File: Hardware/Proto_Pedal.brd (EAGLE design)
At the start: 85.1 x 110.5 mm, 98 parts, among them J1 5.5x2.1mm Barrel, Q1 MMBT2222A, Q2 MOSFET-NCHANNEL2N7002PW, Q3 30V, 2.5A

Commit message: PCB Ready for protos
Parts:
- removed JP68: FX IN, SparkFun-Connectors:1X01NS
- added C2: 100uF, SparkFun-Capacitors:PANASONIC_D
- added D2: RED, SparkFun-LED:LED-0603
- added JP86: FX OUT, SparkFun-Connectors:1X03_NO_SILK
- added JP87: FX IN, SparkFun-Connectors:1X03_NO_SILK
- added LOGO1: SFE_LOGO_NAME_FLAME.2_INCH, SparkFun-Aesthetics:SFE_LOGO_NAME_FLAME_.2
- added LOGO3: OSHW-LOGOL, SparkFun-Aesthetics:OSHW-LOGO-L
- added R4, R5: 100k, SparkFun-Resistors:0603-RES
- added SJ1: disable LED, SparkFun-Passives:PAD-JUMPER-2-NC_BY_PASTE_YES_SILK_FULL_BOX
- added STANDOFF1, STANDOFF2, STANDOFF3, STANDOFF4: STAND-OFF, SparkFun-Electromechanical:STAND-OFF
- JP1: value AUDIO-JACK4-.25-HORIZ-TRS -> INPUT JACK
- JP2: value AUDIO-JACK4-.25-HORIZ-TRS -> OUTPUT JACK
- JP69: value FX OUT -> (none); device SparkFun-Connectors:1X01NS -> SparkFun-Connectors:1X03_NO_SILK
- S1: value (none) -> DPDT Stomp
- U1: value (none) -> TLE2426
- moved JP69 68.1 mm to (40.6, 94.0), turned to 270 degrees
- moved Q1 8.89 mm to (57.1, 7.62)
- moved R1 7.62 mm to (57.1, 14.0)
- moved C1 7.18 mm to (26.7, 104.1)
- moved D1 6.35 mm to (57.1, 3.81)
- moved Q3 5.68 mm to (40.6, 104.1)
- moved JP67 5.08 mm to (67.3, 22.9), turned to 90 degrees
- moved R3 3.59 mm to (36.8, 101.6)
- moved U1 2.84 mm to (31.8, 104.1), turned to 0 degrees
- moved JP66 2.54 mm to (3.81, 72.4)
- moved JP72 2.54 mm to (3.81, 83.8)
- moved JP73 2.54 mm to (16.5, 83.8)
- moved JP75 2.54 mm to (29.2, 83.8)
- moved JP78 2.54 mm to (2.54, 50.8)
- moved JP79 2.54 mm to (41.9, 83.8)
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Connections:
- new net N$25: D2.A, SJ1.2
- net FX_IN: now also JP87.1, JP87.2, JP87.3, R5.2; no longer JP68.1
- net FX_OUT: now also JP86.1, JP86.2, JP86.3, R4.2; no longer JP69.1
- net GND: now also C2.-, JP69.1, R4.1, R5.1
- net LEDA: now also SJ1.1
- net LEDK: now also D2.C
- net VCC: now also C2.+, JP69.3
- net VREF: now also JP69.2
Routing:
- net VCC: track 0.00 -> 350.0 mm, vias 0 -> 3
- net GND: track 0.00 -> 190.0 mm, vias 0 -> 52
- net N$71: track 0.00 -> 184.5 mm, vias 0 -> 1
- net VBATT: track 0.00 -> 174.3 mm
- net N$69: track 0.00 -> 165.8 mm, vias 0 -> 1
- net N$70: track 0.00 -> 121.7 mm, vias 0 -> 1
- net VREF: track 0.00 -> 96.6 mm, vias 0 -> 1
- net FX_IN: track 0.00 -> 77.1 mm
- net N$90: track 0.00 -> 73.7 mm
- net N$89: track 0.00 -> 73.7 mm
- net FX_OUT: track 0.00 -> 58.7 mm
- net N$76: track 0.00 -> 28.7 mm, vias 0 -> 1
- net LEDK: track 0.00 -> 26.6 mm, vias 0 -> 1
- net LEDA: track 0.00 -> 24.4 mm, vias 0 -> 1
- net N$65: track 0.00 -> 21.2 mm
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- added copper zone on layer 1, net GND
- added copper zone on layer 16, net GND
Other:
- outline, holes or cut-outs redrawn
- board text added: "Clear SJ1 to disable SMT LED"
- board text added: "Proto Pedal"
- board text added: "SJ1"
- board text removed: "LEDA"
- board text removed: "LEDK"

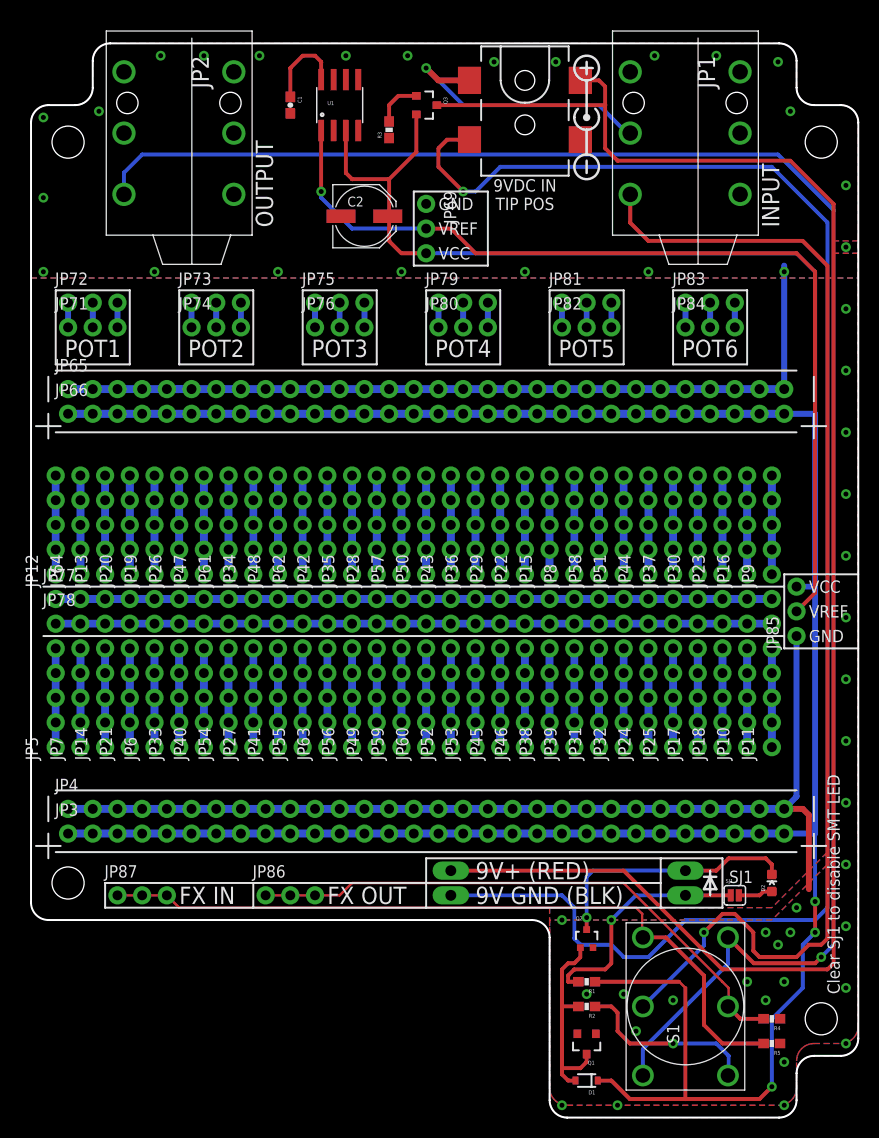
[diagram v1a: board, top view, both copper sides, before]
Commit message: WIP.
Redid bypass switch to 3PDT component with multiple gates.
Removed questionable LED circuit, replaced with an actual switch
section.
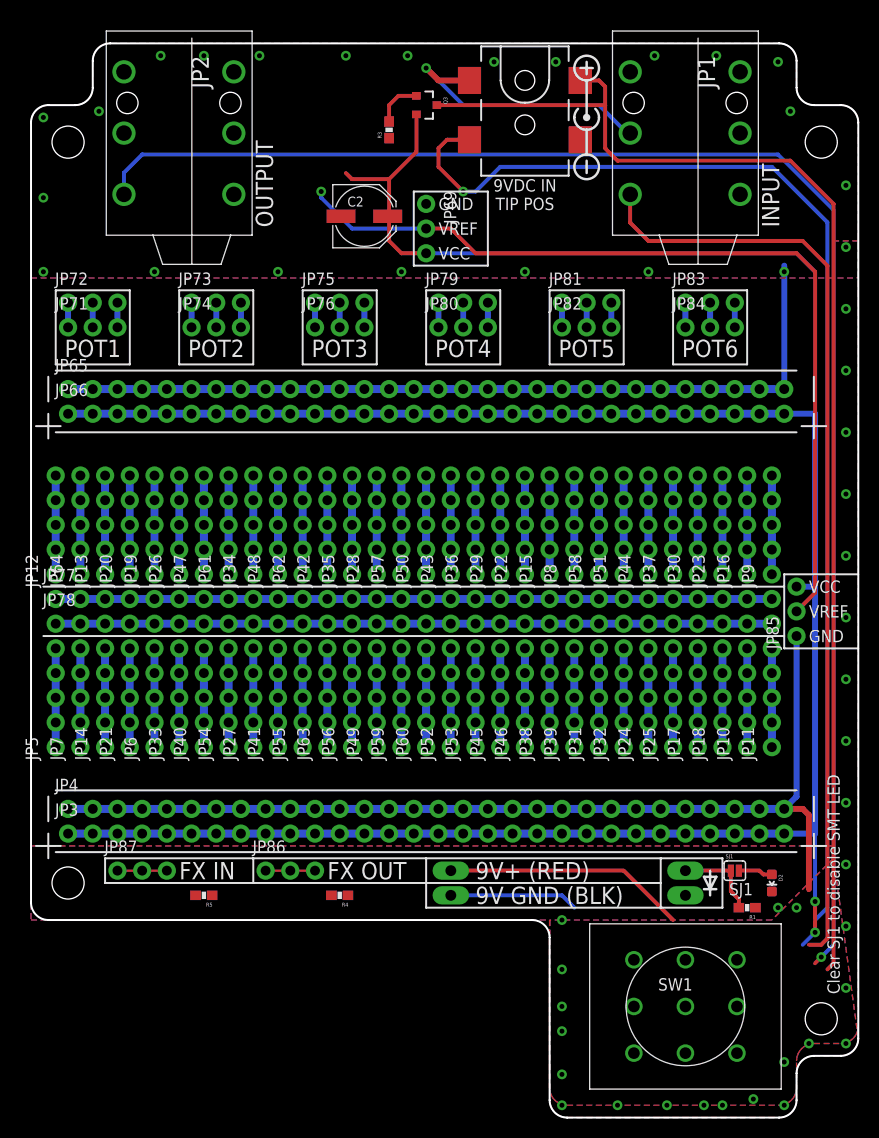
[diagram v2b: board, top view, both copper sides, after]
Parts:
- removed C1: 1.0uF, SparkFun-Capacitors:0603-CAP
- removed D1: BAS16, SparkFun-DiscreteSemi:SOD-323
- removed Q1: MMBT2222A, SparkFun-DiscreteSemi:SOT23-3
- removed Q2: MOSFET-NCHANNEL2N7002PW, SparkFun-DiscreteSemi:SOT323
- removed R2: 10K, SparkFun-Resistors:0603-RES
- removed S1: DPDT Stomp, SparkFun-Electromechanical:STOMP-SWITCH-DPDT
- removed U1: TLE2426, SparkFun-PowerIC:SO08
- added SW1: SWITCH-3PDT, SparkFun-Electromechanical:STOMP-SWITCH-3PDT
- JP3, JP4, JP65, JP66, JP77, JP78: value M30NO_SILK -> (none)
- Q3: value 30V, 2.5A -> 2.5A/30V
- moved R5 60.4 mm to (17.8, 22.9)
- moved R4 46.2 mm to (31.8, 22.9)
- moved R1 18.2 mm to (73.7, 21.6)
- moved JP67 2.54 mm to (67.3, 25.4), turned to 270 degrees
- moved JP86 2.54 mm to (24.1, 25.4)
- moved JP87 2.54 mm to (8.89, 25.4)
- moved SJ1 2.54 mm to (72.4, 25.4)
- turned D2 to 180 degrees
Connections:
- removed net LEDK: D2.C, JP67.2, Q2.3
- removed net N$65: D1.A, Q1.3, Q2.1, R2.2
- removed net N$74: R2.1, S1.P$4
- removed net N$92: C1.1, U1.8
- new net N$35: R1.1, SW1.P$9
- net FX_IN: now also SW1.P$2; no longer S1.P$3
- net FX_OUT: no longer S1.P$5
- net GND: now also D2.C, JP67.2, SW1.P$1; no longer C1.2, Q1.1, Q2.2, U1.2
- net N$70: now also SW1.P$3; no longer S1.P$2
- net N$71: now also SW1.P$5; no longer S1.P$1, S1.P$6
- net VCC: no longer D1.C, R1.1, U1.3
- net VREF: no longer U1.1
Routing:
- net FX_IN: track 77.1 -> 5.08 mm
- net VCC: track 350.0 -> 289.5 mm, vias 3 -> 2
- net FX_OUT: track 58.7 -> 5.08 mm
- net N$69: track 165.8 -> 135.4 mm
- net N$71: track 184.5 -> 156.6 mm
- net LEDK: track 26.6 -> 0.00 mm, vias 1 -> 0
- net N$70: track 121.7 -> 96.4 mm, vias 1 -> 0
- net N$65: track 21.2 -> 0.00 mm
- net N$74: track 19.0 -> 0.00 mm, vias 1 -> 0
- net VBATT: track 174.3 -> 156.3 mm
- net LEDA: track 24.4 -> 8.82 mm, vias 1 -> 0
- net N$92: track 8.75 -> 0.00 mm
- net VREF: track 96.6 -> 90.3 mm

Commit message: More WIP
Many more changes based on prototype review.
-Tip-negative power input.
-uncommited proto space for power regulation.
-Rail splitter removed
-Strain relief near 9V snap
-Some test points on i/O jacks
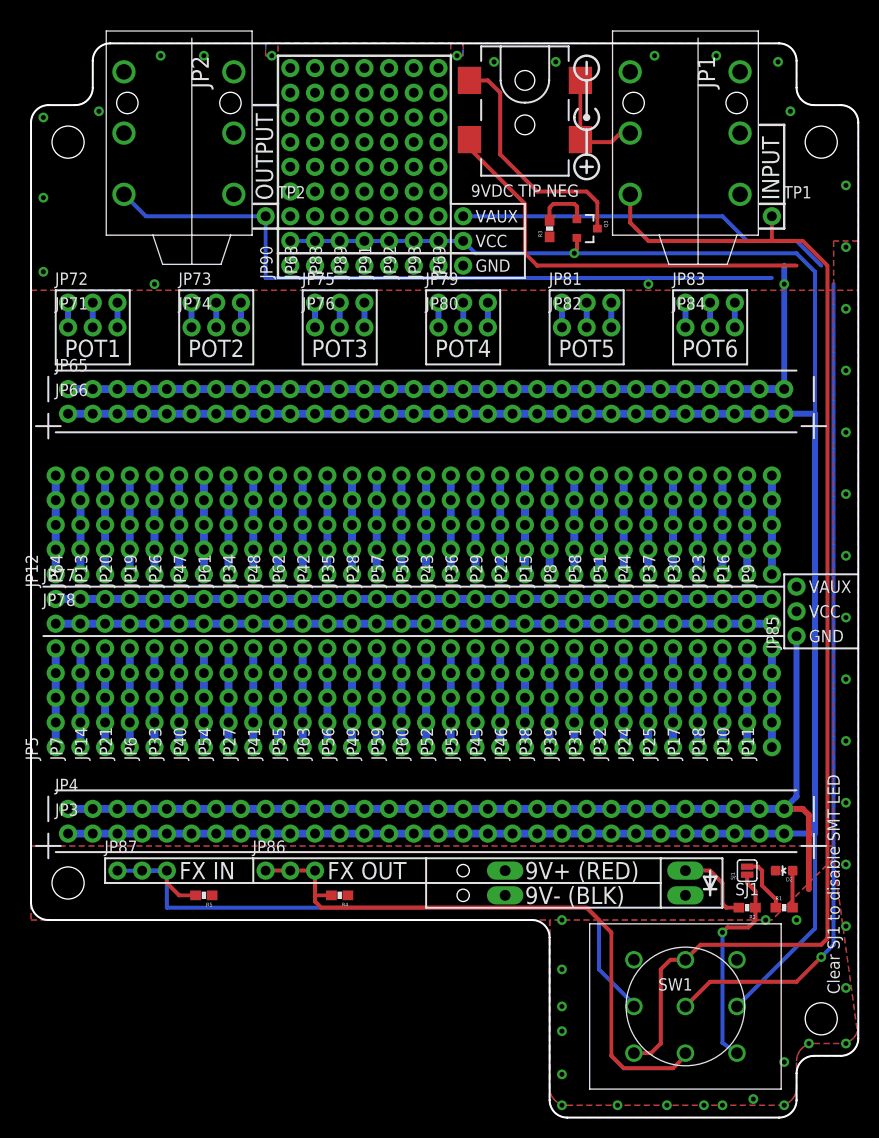
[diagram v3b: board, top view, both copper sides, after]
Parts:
- removed C2: 100uF, SparkFun-Capacitors:PANASONIC_D
- added JP68, JP88, JP89, JP90, JP91, JP92, JP93: (no value), SparkFun-Connectors:1X09_NO_SILK
- added R2: 1K, SparkFun-Resistors:0603-RES
- added TP1: Raw In, SparkFun-Connectors:1X01_NO_SILK
- added TP2: Raw Out, SparkFun-Connectors:1X01_NO_SILK
- J1: value 5.5x2.1mm Barrel -> POWER_JACKSMD_FIXED; device SparkFun-Connectors:POWER_JACK_SMD -> Testing:POWER_JACK_SMD
- moved Q3 20.8 mm to (57.1, 91.4)
- moved R3 19.4 mm to (53.3, 91.4)
- moved LOGO1 17.0 mm to (53.3, 114.3)
- moved JP69 7.41 mm to (44.5, 87.6), turned to 90 degrees
- moved JP70 5.59 mm to (48.8, 25.4)
- moved R1 3.81 mm to (77.5, 21.6), turned to 0 degrees
- moved D2 1.80 mm to (77.5, 25.4), turned to 90 degrees
- moved SJ1 1.27 mm to (73.7, 25.4), turned to 90 degrees
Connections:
- removed net N$69: J1.P$4, JP70.2
- removed net N$76: J1.GND, JP1.RING
- removed net VREF: JP69.2, JP85.2
- new net N$45: J1.P$4, JP70.1
- new net N$55: J1.VIN0, J1.VIN1, JP1.RING, JP70.2
- new net N$65: R1.1, SJ1.2
- new net VAUX: JP69.3, JP85.3
- net FX_OUT: now also SW1.P$6
- net GND: now also JP68.1, JP88.1, JP89.1, JP90.1, JP91.1, JP92.1, JP93.1; no longer C2.-
- net LEDA: now also R2.2; no longer R1.2, SJ1.1
- net N$25: now also R1.2; no longer SJ1.2
- net N$35: now also R2.1, SJ1.1; no longer R1.1
- net N$70: now also SW1.P$4, TP1.1
- net N$71: now also TP2.1
- net VBATT: now also J1.GND; no longer J1.VIN0, JP70.1
- net VCC: now also JP68.2, JP69.2, JP85.2, JP88.2, JP89.2, JP90.2, JP91.2, JP92.2, JP93.2, SW1.P$8; no longer C2.+, JP69.3, JP85.3
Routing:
- net N$69: track 135.4 -> 0.00 mm, vias 1 -> 0
- net VBATT: track 156.3 -> 24.8 mm
- net VREF: track 90.3 -> 0.00 mm, vias 1 -> 0
- net FX_IN: track 5.08 -> 71.5 mm
- net FX_OUT: track 5.08 -> 63.4 mm
- net N$45: track 0.00 -> 42.5 mm
- net VAUX: track 0.00 -> 38.9 mm
- net N$70: track 96.4 -> 126.0 mm
- net N$76: track 28.7 -> 0.00 mm, vias 1 -> 0
- net N$35: track 0.00 -> 22.2 mm, vias 0 -> 1
- net N$55: track 0.00 -> 11.7 mm
- net N$65: track 0.00 -> 6.10 mm
- net N$71: track 156.6 -> 159.7 mm
- net N$75: track 4.89 -> 5.71 mm
- net VCC: track 289.5 -> 289.6 mm, vias 2 -> 1
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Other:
- board text added: "9V- (BLK)"
- board text added: "9VDC IN TIP NEG"
- board text added: "9VDC TIP NEG"
- board text added: "VAUX"
- board text removed: "9V GND (BLK)"
- board text removed: "9VDC IN TIP POS"
- board text removed: "VREF"

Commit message: More WIP.
-Columns labeled.
-Traces complete.
-Text & silk more complete & organized.
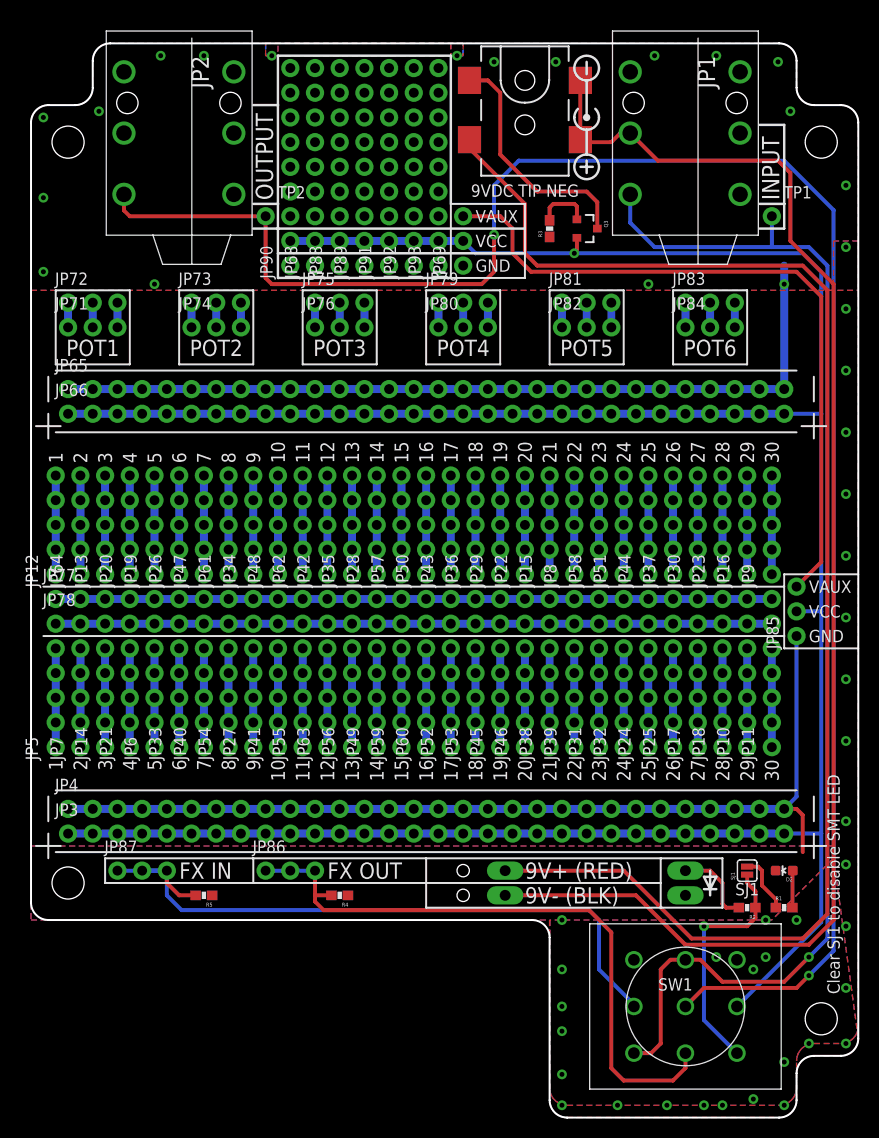
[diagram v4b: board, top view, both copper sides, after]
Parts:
- moved LOGO1 41.3 mm to (83.2, 85.7)
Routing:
- net N$55: track 11.7 -> 145.5 mm
- net N$45: track 42.5 -> 148.0 mm
- net VAUX: track 38.9 -> 72.6 mm
- net N$71: track 159.7 -> 187.9 mm, vias 1 -> 2
- net VCC: track 289.6 -> 294.3 mm
- net GND: track 190.0 -> 185.6 mm, vias 48 -> 51
- net N$35: track 22.2 -> 24.9 mm
- net FX_OUT: track 63.4 -> 65.9 mm
- net N$70: track 126.0 -> 128.5 mm, vias 0 -> 1
- net FX_IN: track 71.5 -> 70.8 mm
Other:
- board text added: "1"
- board text added: "10"
- board text added: "11"
- board text added: "12"
- board text added: "13"
- board text added: "14"
- board text added: "15"
- board text added: "16"
- board text added: "17"
- board text added: "18"
- board text added: "19"
- board text added: "2"
- board text added: "20"
- board text added: "21"
- board text added: "22"
- board text added: "23"
- board text added: "24"
- board text added: "25"
- board text added: "26"
- board text added: "27"
- board text added: "28"
- board text added: "29"
- board text added: "3"
- board text added: "30"
- board text added: "4"
- board text added: "5"
- board text added: "6"
- board text added: "7"
- board text added: "8"
- board text added: "9"

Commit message: More WIP
Much cleanup for review soon.
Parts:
- removed JP67: LED, SparkFun-Connectors:1X02_LONGPADS
- added C1: C in, Testing:DUAL-CAP
- added C2: C out, Testing:DUAL-CAP
- added D1: RED, SparkFun-LED:LED-0603
- added FID1, FID2: FIDUCIAL1X2, SparkFun-Aesthetics:FIDUCIAL-1X2
- added JP94, JP95, JP96: 1x2, SparkFun-Connectors:1X02_NO_SILK
- added TP3: Out Ring, SparkFun-Connectors:1X01_NO_SILK
- added TP4: In Ring, SparkFun-Connectors:1X01_NO_SILK
- added TP5: FX Input, SparkFun-Connectors:1X01_NO_SILK
- added TP6: FX Output, SparkFun-Connectors:1X01_NO_SILK
- D2: value RED -> PTH-LED; device SparkFun-LED:LED-0603 -> SparkFun-Connectors:1X02_LONGPADS
- JP10, JP11, JP12, JP13, JP14, JP15, JP16, JP17, JP18, JP19, JP20, JP21, JP22, JP23, JP24, JP25, JP26, JP27, JP28, JP29, JP30, JP31, JP32, JP33, JP34, JP35, JP36, JP37, JP38, JP39, JP40, JP41, JP42, JP43, JP44, JP45, JP46, JP47, JP48, JP49, JP5, JP50, JP51, JP52, JP53, JP54, JP56, JP57, JP58, JP59, JP6, JP60, JP61, JP62, JP63, JP64, JP7, JP8, JP9: value (none) -> 1x5
- JP3, JP4, JP65, JP66, JP77, JP78: value (none) -> 1x30
- JP55: value (none) -> v
- JP68, JP88, JP89, JP90, JP91, JP92, JP93: value (none) -> 1x9
- JP69, JP71, JP72, JP73, JP74, JP75, JP76, JP79, JP80, JP81, JP82, JP83, JP84, JP85: value (none) -> 1x3
- JP86: value FX OUT -> 1x2; device SparkFun-Connectors:1X03_NO_SILK -> SparkFun-Connectors:1X02_NO_SILK
- JP87: value FX IN -> 1x2; device SparkFun-Connectors:1X03_NO_SILK -> SparkFun-Connectors:1X02_NO_SILK
- R1, R2, R3: device SparkFun-Resistors:0603-RES -> SparkFun-Resistors:0603-RES@1
- R4, R5: value 100k -> 1M
- moved JP87 100.2 mm to (66.7, 107.3)
- moved JP86 82.5 mm to (14.6, 107.3)
- moved D2 10.2 mm to (67.3, 25.4), turned to 270 degrees
- moved R4 2.54 mm to (29.2, 22.9), turned to 0 degrees
- moved R5 1.90 mm to (19.7, 22.9)
- renumbered Q3 to Q1
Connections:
- new net N$66: JP2.RING, TP3.1
- new net N$67: C1.P$1, TP5.1
- new net N$68: C2.P$1, TP6.1
- net FX_IN: now also C1.P$2, C1.P$3; no longer JP87.1, JP87.2, JP87.3
- net FX_OUT: now also C2.P$2, C2.P$3; no longer JP86.1, JP86.2, JP86.3
- net GND: now also D1.C, D2.2, JP86.1, JP86.2, JP87.1, JP87.2, JP94.1, JP94.2, JP95.1, JP95.2, JP96.1, JP96.2; no longer D2.C, JP67.2
- net LEDA: now also D2.1; no longer JP67.1
- net N$25: now also D1.A; no longer D2.A
- net N$55: now also TP4.1
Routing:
- net N$66: track 0.00 -> 7.45 mm
- net N$67: track 0.00 -> 4.44 mm
- net N$68: track 0.00 -> 3.81 mm
- net FX_OUT: track 65.9 -> 62.5 mm
- net FX_IN: track 70.8 -> 72.0 mm
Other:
- board text added: "IN->OUT"
- board text added: "OUT<-IN"
- board text added: "V02"
- board text removed: "FX IN"
- board text removed: "FX OUT"

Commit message: Preparing for review
Lots of little touch ups.
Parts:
- R1, R2, R3: device SparkFun-Resistors:0603-RES@1 -> SparkFun-Resistors:0603-RES
- moved JP86 2.01 mm to (14.0, 109.2)
- moved JP87 2.01 mm to (66.0, 109.2)
- moved JP95 1.27 mm to (54.6, 10.2)
- moved JP94 0.90 mm to (1.27, 92.7)
- moved JP96 0.63 mm to (83.8, 94.0)
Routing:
- net GND: vias 51 -> 58
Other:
- board text added: "All Dimensions in inches"
- board text added: "BYPASS SWITCH"
- board text added: "LED hole to match component. 3mm or 5mm are common."
- board text added: "Power jack needs minimum 0.25" hole, possibly larger to allow for plug jacket."
- board text added: "Stomp switch needs 0.5" hole"
- board text added: "TRS Jacks need 2x 0.4" holes"
